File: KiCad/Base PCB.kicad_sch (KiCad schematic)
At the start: 8 parts, among them J3 Conn_02x32_Odd_Even, J4 Conn_02x20_Odd_Even

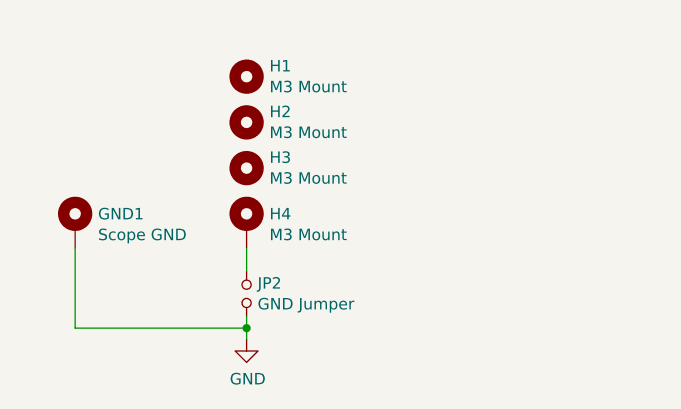
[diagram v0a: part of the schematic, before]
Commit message: Changed Pin Mapping
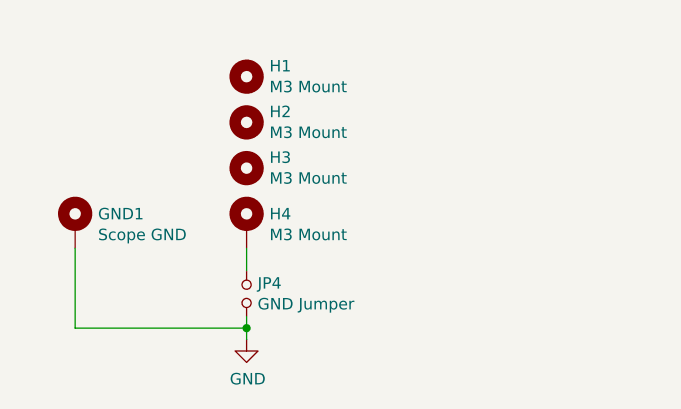
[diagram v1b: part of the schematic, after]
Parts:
- renumbered JP2 to JP4
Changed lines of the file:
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@@
   (symbol (lib_id "Device:Jumper_NO_Small") (at 50.8 172.72 270) (unit 1)
     (in_bom yes) (on_board yes)
-    (property "Reference" "JP2" (id 0) (at 52.0192 171.5516 90)
+    (property "Reference" "JP4" (id 0) (at 52.0192 171.5516 90)
       (effects (font (size 1.27 1.27)) (justify left))
     )

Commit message: Schematic and BOM Checked
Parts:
- renumbered JP4 to JP5
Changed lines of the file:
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@@
   (symbol (lib_id "Device:Jumper_NO_Small") (at 50.8 172.72 270) (unit 1)
     (in_bom yes) (on_board yes)
-    (property "Reference" "JP4" (id 0) (at 52.0192 171.5516 90)
+    (property "Reference" "JP5" (id 0) (at 52.0192 171.5516 90)
       (effects (font (size 1.27 1.27)) (justify left))
     )
